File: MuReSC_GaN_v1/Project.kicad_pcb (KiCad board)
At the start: 2 copper layers, 19 parts, among them IC1 STM32G474RET6, IC10 UCC12040DVE, IC2 TPSM5601R5HRDAR, IC3 ISO7720FQDQ1, IC4 ISO7720FQDQ1, IC5 ISO7720FQDQ1, IC6 ISO7720FQDQ1, IC7 UCC12040DVE, IC8 UCC12040DVE, IC9 UCC12040DVE, J1 62000211121, J2 62000211121, J3 691214110002, J4 691214110002, J5 691214110002, J6 691214110002

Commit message: finito schema
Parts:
- removed J5, J6: 691214110002, SamacSys_Parts:691214110002
- added BEAD1: BLM15AG601SZ1D, SamacSys_Parts:NFZ15SG152SN10B, F.Cu at (131.7, 147.4)
- added BEAD2: BLM15AG601SZ1D, SamacSys_Parts:NFZ15SG152SN10B, F.Cu at (131.7, 149.9)
- added C1: C1812C124J1GACTU, SamacSys_Parts:C1812, F.Cu at (127.5, 136.8)
- added C2: C1206C821J1GACTU, SamacSys_Parts:C1206, F.Cu at (100.9, 148.9)
- added C3: C1812C105K1RACTU, SamacSys_Parts:C1812, F.Cu at (127.5, 143.1)
- added CCV1: C1210C107M8PACTU, SamacSys_Parts:C1210, F.Cu at (113.3, 92.3)
- added CCV2: C1210C107M8PACTU, SamacSys_Parts:C1210, F.Cu at (113.3, 97.9)
- added CD1: GRT155R70J105KE01D, SamacSys_Parts:CAPC1005X55N, F.Cu at (106.6, 130.3)
- added CD2: GRT155R70J105KE01D, SamacSys_Parts:CAPC1005X55N, F.Cu at (106.6, 132.3)
- added CD3: GRT155R70J105KE01D, SamacSys_Parts:CAPC1005X55N, F.Cu at (106.6, 134.3)
- added CD4: GRT155R70J105KE01D, SamacSys_Parts:CAPC1005X55N, F.Cu at (106.6, 136.2)
- added CFT1: NFM15PC104R1A3D, SamacSys_Parts:NFM15CC222D1A3D, F.Cu at (132.3, 109.8)
- added CFT2: NFM15PC104R1A3D, SamacSys_Parts:NFM15CC222D1A3D, F.Cu at (132.3, 112.6)
- added CFT3: NFM15PC104R1A3D, SamacSys_Parts:NFM15CC222D1A3D, F.Cu at (132.3, 115.5)
- added CFT4: NFM15PC104R1A3D, SamacSys_Parts:NFM15CC222D1A3D, F.Cu at (132.3, 118.3)
- added CIN1: GRJ31CZ72A475KE01L, SamacSys_Parts:CAPC3216X190N, F.Cu at (119.3, 91.2)
- added CIN2: GRJ31CZ72A475KE01L, SamacSys_Parts:CAPC3216X190N, F.Cu at (119.3, 94.5)
- added CISOP1: GRT155R70J105KE01D, SamacSys_Parts:CAPC1005X55N, F.Cu at (106.6, 138.2)
- added CISOP2: GRT155R70J105KE01D, SamacSys_Parts:CAPC1005X55N, F.Cu at (106.6, 140.2)
- added CISOP3: GRT155R70J105KE01D, SamacSys_Parts:CAPC1005X55N, F.Cu at (106.6, 142.2)
- added CISOP4: GRT155R70J105KE01D, SamacSys_Parts:CAPC1005X55N, F.Cu at (106.6, 144.1)
- added CISOS1: GRT155R70J105KE01D, SamacSys_Parts:CAPC1005X55N, F.Cu at (109.5, 130.3)
- added CISOS2: GRT155R70J105KE01D, SamacSys_Parts:CAPC1005X55N, F.Cu at (109.5, 132.3)
- added CISOS3: GRT155R70J105KE01D, SamacSys_Parts:CAPC1005X55N, F.Cu at (109.5, 134.3)
- added CISOS4: GRT155R70J105KE01D, SamacSys_Parts:CAPC1005X55N, F.Cu at (109.5, 136.2)
- added CLD1: GRM155Z71A105KE01J, SamacSys_Parts:CAPC1005X55N, F.Cu at (121.5, 97.1)
- added CLD2: GRT155R70J105KE01D, SamacSys_Parts:CAPC1005X55N, F.Cu at (121.5, 99.1)
- added CM0: GRM155R61A475MEAAD, SamacSys_Parts:CAPC1005X55N, F.Cu at (109.5, 138.2)
- added CM1: C0402C104K8RAC7867, SamacSys_Parts:CAPC1005X55N, F.Cu at (109.5, 140.2)
- added CM10: C0402C104K8RAC7867, SamacSys_Parts:CAPC1005X55N, F.Cu at (112.4, 142.2)
- added CM2: C0402C104K8RAC7867, SamacSys_Parts:CAPC1005X55N, F.Cu at (109.5, 142.2)
- added CM3: C0402C104K8RAC7867, SamacSys_Parts:CAPC1005X55N, F.Cu at (109.5, 144.1)
- added CM4: C0402C104K8RAC7867, SamacSys_Parts:CAPC1005X55N, F.Cu at (112.4, 130.3)
- added CM5: GRT155R70J105KE01D, SamacSys_Parts:CAPC1005X55N, F.Cu at (112.4, 132.3)
- added CM6: C0402C104K8RAC7867, SamacSys_Parts:CAPC1005X55N, F.Cu at (112.4, 134.3)
- added CM7: C0402C104K8RAC7867, SamacSys_Parts:CAPC1005X55N, F.Cu at (112.4, 136.2)
- added CM8: GRT155R70J105KE01D, SamacSys_Parts:CAPC1005X55N, F.Cu at (112.4, 138.2)
- added CM9: C0402C104K8RAC7867, SamacSys_Parts:CAPC1005X55N, F.Cu at (112.4, 140.2)
- added COH1: GJM0335C1E6R8DB01D, SamacSys_Parts:CAPC0603X33N, F.Cu at (113.1, 148.5)
- added COH2: GJM0335C1E6R8DB01D, SamacSys_Parts:CAPC0603X33N, F.Cu at (113.1, 150.3)
- added COL1: C, Capacitor_SMD:C_0201_0603Metric_Pad0.64x0.40mm_HandSolder, F.Cu at (93.7, 146.8)
- added COL2: C, Capacitor_SMD:C_0201_0603Metric_Pad0.64x0.40mm_HandSolder, F.Cu at (93.7, 148.6)
- added CTP1: C0402C104K8RAC7867, SamacSys_Parts:CAPC1005X55N, F.Cu at (112.4, 144.1)
- added CTP2: C0402C104K8RAC7867, SamacSys_Parts:CAPC1005X55N, F.Cu at (115.2, 130.3)
- added CTP3: C0402C104K8RAC7867, SamacSys_Parts:CAPC1005X55N, F.Cu at (115.2, 132.3)
- added CTP4: C0402C104K8RAC7867, SamacSys_Parts:CAPC1005X55N, F.Cu at (115.2, 134.3)
- added CTPB1: C0603C106M8PAC7411, SamacSys_Parts:C0603, F.Cu at (94.9, 110.3)
- added CTPB2: C0603C106M8PAC7411, SamacSys_Parts:C0603, F.Cu at (94.9, 114.1)
- added CTPB3: C0603C106M8PAC7411, SamacSys_Parts:C0603, F.Cu at (94.9, 118.0)
- added CTPB4: C0603C106M8PAC7411, SamacSys_Parts:C0603, F.Cu at (94.9, 121.8)
- added CTS1: C0402C104K8RAC7867, SamacSys_Parts:CAPC1005X55N, F.Cu at (115.2, 136.2)
- added CTS2: C0402C104K8RAC7867, SamacSys_Parts:CAPC1005X55N, F.Cu at (115.2, 138.2)
- added CTS3: C0402C104K8RAC7867, SamacSys_Parts:CAPC1005X55N, F.Cu at (115.2, 140.2)
- added CTS4: C0402C104K8RAC7867, SamacSys_Parts:CAPC1005X55N, F.Cu at (115.2, 142.2)
- added CTSB1: C0603C106M8PAC7411, SamacSys_Parts:C0603, F.Cu at (94.9, 125.7)
- added CTSB2: C0603C106M8PAC7411, SamacSys_Parts:C0603, F.Cu at (94.9, 129.5)
- added CTSB3: C0603C106M8PAC7411, SamacSys_Parts:C0603, F.Cu at (94.9, 133.4)
- added CTSB4: C0603C106M8PAC7411, SamacSys_Parts:C0603, F.Cu at (94.9, 137.2)
- added D1: ESDALC6V1-1U2, SamacSys_Parts:ESDALC6V11U2, F.Cu at (94.5, 140.9)
- added D2: ESDALC6V1-1U2, SamacSys_Parts:ESDALC6V11U2, F.Cu at (94.5, 144.3)
- added IC11: LMG1020YFFR, SamacSys_Parts:BGA6C40P2X3_86X126X62, F.Cu at (118.6, 131.5)
- added IC12: LMG1020YFFR, SamacSys_Parts:BGA6C40P2X3_86X126X62, F.Cu at (122.6, 131.5)
- added IC13: LMG1020YFFR, SamacSys_Parts:BGA6C40P2X3_86X126X62, F.Cu at (126.5, 131.5)
- added IC14: LMG1020YFFR, SamacSys_Parts:BGA6C40P2X3_86X126X62, F.Cu at (130.5, 131.5)
- added L1: L, Inductor_SMD:L_0603_1608Metric, F.Cu at (113.9, 146.4)
- added P1: 691214110002, SamacSys_Parts:691214110002, F.Cu at (108.7, 113.9)
- added P2: 691214110002, SamacSys_Parts:691214110002, F.Cu at (108.7, 124.4)
- added Q1: GS61004B-TR, SamacSys_Parts:GS61004BTR, F.Cu at (101.3, 112.1)
- added Q2: GS61004B-TR, SamacSys_Parts:GS61004BTR, F.Cu at (101.3, 119.6)
- added Q3: GS61004B-TR, SamacSys_Parts:GS61004BTR, F.Cu at (101.3, 127.1)
- added Q4: GS61004B-TR, SamacSys_Parts:GS61004BTR, F.Cu at (101.3, 134.6)
- added RF1: MCS04020D1002BE000, SamacSys_Parts:RESC1005X37N, F.Cu at (118.3, 97.2)
- added RF2: MCS04020D2491BE000, SamacSys_Parts:RESC1005X37N, F.Cu at (118.3, 99.3)
- added RH1: MCS0402MC1008FE000, SamacSys_Parts:RESC1005X37N, F.Cu at (118.4, 134.8)
- added RH2: MCS0402MC1008FE000, SamacSys_Parts:RESC1005X37N, F.Cu at (118.4, 136.9)
- added RH3: MCS0402MC1008FE000, SamacSys_Parts:RESC1005X37N, F.Cu at (118.4, 139.1)
- added RH4: MCS0402MC1008FE000, SamacSys_Parts:RESC1005X37N, F.Cu at (118.4, 141.2)
- added RL1: MCS0402MC1008FE000, SamacSys_Parts:RESC1005X37N, F.Cu at (118.4, 143.4)
- added RL2: MCS0402MC1008FE000, SamacSys_Parts:RESC1005X37N, F.Cu at (118.4, 145.5)
- added RL3: MCS0402MC1008FE000, SamacSys_Parts:RESC1005X37N, F.Cu at (121.7, 134.8)
- added RL4: MCS0402MC1008FE000, SamacSys_Parts:RESC1005X37N, F.Cu at (121.7, 136.9)
- added RM1: MCS04020D1002BE000, SamacSys_Parts:RESC1005X37N, F.Cu at (121.7, 139.1)
- added RS1: R, Resistor_SMD:R_0603_1608Metric_Pad0.98x0.95mm_HandSolder, F.Cu at (117.9, 109.6)
- added RS2: R, Resistor_SMD:R_0603_1608Metric_Pad0.98x0.95mm_HandSolder, F.Cu at (117.9, 112.1)
- added RS3: R, Resistor_SMD:R_0603_1608Metric_Pad0.98x0.95mm_HandSolder, F.Cu at (117.9, 114.6)
- added RS4: R, Resistor_SMD:R_0603_1608Metric_Pad0.98x0.95mm_HandSolder, F.Cu at (117.9, 117.1)
- added RS5: R, Resistor_SMD:R_0603_1608Metric_Pad0.98x0.95mm_HandSolder, F.Cu at (117.9, 119.7)
- added RS6: R, Resistor_SMD:R_0603_1608Metric_Pad0.98x0.95mm_HandSolder, F.Cu at (117.9, 122.2)
- added RS7: R, Resistor_SMD:R_0603_1608Metric_Pad0.98x0.95mm_HandSolder, F.Cu at (117.9, 124.7)
- added RS8: R, Resistor_SMD:R_0603_1608Metric_Pad0.98x0.95mm_HandSolder, F.Cu at (117.9, 127.2)
- added RUB1: MCS04020C3300FE000, SamacSys_Parts:RESC1005X37N, F.Cu at (121.7, 141.2)
- added RUB2: MCS04020C1003FE000, SamacSys_Parts:RESC1005X37N, F.Cu at (121.7, 143.4)
- added S1: PTS526_SK15_SMTR2_LFS, SamacSys_Parts:PTS526SK15SMTR2LFS, F.Cu at (125.6, 112.5)
- added S2: PTS526_SK15_SMTR2_LFS, SamacSys_Parts:PTS526SK15SMTR2LFS, F.Cu at (125.6, 120.8)
- added Y1: NX3215SA-32.768K-STD-MUS-2, SamacSys_Parts:NX3215SA32768KSTDMUS2, F.Cu at (126.7, 148.6)
- added Y2: NX3225SA-24.000MHZ-STD-CSR-1, SamacSys_Parts:NX3225SA24000MHZSTDCSR1, F.Cu at (108.5, 148.1)
- added Z3: TSZU52C3V3_RGG, SamacSys_Parts:TSZU52C3V3RGG, F.Cu at (100.0, 140.4)
- added Z4: TSZU52C3V3_RGG, SamacSys_Parts:TSZU52C3V3RGG, F.Cu at (100.0, 144.5)
- J1: value 62000211121 -> 62000211121_x6; footprint SamacSys_Parts:62000211121 -> SamacSys_Parts:62000211121_x6
- J3, J4: value 691214110002 -> 62000211121_x1; footprint SamacSys_Parts:691214110002 -> SamacSys_Parts:62000211121_x1
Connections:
- IC1 pad 1: unconnected-(IC1-VBAT-Pad1) -> /VDD3V3
- IC1 pad 12: unconnected-(IC1-PA0-Pad12) -> /ADC1_IN1
- IC1 pad 13: unconnected-(IC1-PA1-Pad13) -> /ADC2_IN2
- IC1 pad 14: unconnected-(IC1-PA2-Pad14) -> /STLINK_RX
- IC1 pad 15: unconnected-(IC1-VSS_1-Pad15) -> GND
- IC1 pad 16: unconnected-(IC1-VDD_1-Pad16) -> /VDD3V3
- IC1 pad 17: unconnected-(IC1-PA3-Pad17) -> /STLINK_TX
- IC1 pad 18: unconnected-(IC1-PA4-Pad18) -> /COMP1_INM
- IC1 pad 19: unconnected-(IC1-PA5-Pad19) -> /COMP2_INM
- IC1 pad 2: unconnected-(IC1-PC13-Pad2) -> /UBUTT
- IC1 pad 21: unconnected-(IC1-PA7-Pad21) -> /COMP2_INP
- IC1 pad 25: unconnected-(IC1-PB1-Pad25) -> /COMP1_INP
- IC1 pad 27: unconnected-(IC1-VSSA-Pad27) -> GND
- IC1 pad 28: unconnected-(IC1-VREF+-Pad28) -> /VREFP
- IC1 pad 29: unconnected-(IC1-VDDA-Pad29) -> Net-(IC1-VDDA)
- IC1 pad 3: unconnected-(IC1-PC14-OSC32_IN-Pad3) -> /OSC32_IN
- IC1 pad 31: unconnected-(IC1-VSS_2-Pad31) -> GND
- IC1 pad 32: unconnected-(IC1-VDD_2-Pad32) -> /VDD3V3
- IC1 pad 34: unconnected-(IC1-PB12-Pad34) -> /HRTIM1_CHC1
- IC1 pad 35: unconnected-(IC1-PB13-Pad35) -> /HRTIM1_CHC2
- IC1 pad 36: unconnected-(IC1-PB14-Pad36) -> /HRTIM1_CHD1
- IC1 pad 37: unconnected-(IC1-PB15-Pad37) -> /HRTIM1_CHD2
- IC1 pad 4: unconnected-(IC1-PC15-OSC32_OUT-Pad4) -> /OSC32_OUT
- IC1 pad 42: unconnected-(IC1-PA8-Pad42) -> /HRTIM1_CHA1
- IC1 pad 43: unconnected-(IC1-PA9-Pad43) -> /HRTIM1_CHA2
- IC1 pad 44: unconnected-(IC1-PA10-Pad44) -> /HRTIM1_CHB1
- IC1 pad 45: unconnected-(IC1-PA11-Pad45) -> /HRTIM1_CHB2
- IC1 pad 47: unconnected-(IC1-VSS_3-Pad47) -> GND
- IC1 pad 48: unconnected-(IC1-VDD_3-Pad48) -> /VDD3V3
- IC1 pad 49: unconnected-(IC1-PA13-Pad49) -> /T_SWDIO
- IC1 pad 5: unconnected-(IC1-PF0-OSC_IN-Pad5) -> /OSC24_IN
- IC1 pad 50: unconnected-(IC1-PA14-Pad50) -> /T_SWCLK
- IC1 pad 6: unconnected-(IC1-PF1-OSC_OUT-Pad6) -> /OSC24_OUT
- IC1 pad 61: unconnected-(IC1-PB8-BOOT0-Pad61) -> Net-(IC1-PB8-BOOT0)
- IC1 pad 63: unconnected-(IC1-VSS_4-Pad63) -> GND
- IC1 pad 64: unconnected-(IC1-VDD_4-Pad64) -> /VDD3V3
- IC1 pad 7: unconnected-(IC1-PG10-NRST-Pad7) -> /NRST
- IC10 pad 1: unconnected-(IC10-EN-Pad1) -> /VDD5V
- IC10 pad 10: unconnected-(IC10-NC_4-Pad10) -> GND
- IC10 pad 11: unconnected-(IC10-NC_5-Pad11) -> GND
- IC10 pad 12: unconnected-(IC10-NC_6-Pad12) -> GND
- IC10 pad 13: unconnected-(IC10-SEL-Pad13) -> /VDDI4
- IC10 pad 14: unconnected-(IC10-VISO-Pad14) -> /VDDI4
- IC10 pad 15: unconnected-(IC10-GNDS_2-Pad15) -> GND
- IC10 pad 16: unconnected-(IC10-GNDS_3-Pad16) -> GND
- IC10 pad 2: unconnected-(IC10-GNDP-Pad2) -> GND
- IC10 pad 3: unconnected-(IC10-VINP-Pad3) -> /VDD5V
- IC10 pad 4: unconnected-(IC10-SYNC-Pad4) -> GND
- IC10 pad 6: unconnected-(IC10-NC_1-Pad6) -> GND
- IC10 pad 7: unconnected-(IC10-NC_2-Pad7) -> GND
- IC10 pad 8: unconnected-(IC10-NC_3-Pad8) -> GND
- IC10 pad 9: unconnected-(IC10-GNDS_1-Pad9) -> GND
- IC2 pad 1: unconnected-(IC2-VIN_1-Pad1) -> /VDD48V
- IC2 pad 10: unconnected-(IC2-AGND-Pad10) -> GND
- IC2 pad 12: unconnected-(IC2-PGOOD-Pad12) -> GND
- IC2 pad 14: unconnected-(IC2-VIN_2-Pad14) -> /VDD48V
- IC2 pad 2: unconnected-(IC2-EN-Pad2) -> /VDD48V
- IC2 pad 7: unconnected-(IC2-VOUT_1-Pad7) -> /VDD5V
- IC2 pad 8: unconnected-(IC2-VOUT_2-Pad8) -> /VDD5V
- IC2 pad 9: unconnected-(IC2-FB-Pad9) -> /TPSFB
- IC3 pad 1: unconnected-(IC3-VCC1-Pad1) -> /VDD3V3
- IC3 pad 2: unconnected-(IC3-INA-Pad2) -> /HRTIM1_CHA1
- IC3 pad 3: unconnected-(IC3-INB-Pad3) -> /HRTIM1_CHA2
- IC3 pad 4: unconnected-(IC3-GND1-Pad4) -> GND
- IC3 pad 5: unconnected-(IC3-GND2-Pad5) -> /S1
- IC3 pad 6: unconnected-(IC3-OUTB-Pad6) -> /INN1
- IC3 pad 7: unconnected-(IC3-OUTA-Pad7) -> /INP1
- IC3 pad 8: unconnected-(IC3-VCC2-Pad8) -> /VDDI1
- IC4 pad 1: unconnected-(IC4-VCC1-Pad1) -> /VDD3V3
- IC4 pad 2: unconnected-(IC4-INA-Pad2) -> /HRTIM1_CHB1
- IC4 pad 3: unconnected-(IC4-INB-Pad3) -> /HRTIM1_CHB2
- IC4 pad 4: unconnected-(IC4-GND1-Pad4) -> GND
- IC4 pad 5: unconnected-(IC4-GND2-Pad5) -> /S2
- IC4 pad 6: unconnected-(IC4-OUTB-Pad6) -> /INN2
- IC4 pad 7: unconnected-(IC4-OUTA-Pad7) -> /INP2
- IC4 pad 8: unconnected-(IC4-VCC2-Pad8) -> /VDDI2
- IC5 pad 1: unconnected-(IC5-VCC1-Pad1) -> /VDD3V3
- IC5 pad 2: unconnected-(IC5-INA-Pad2) -> /HRTIM1_CHC1
- IC5 pad 3: unconnected-(IC5-INB-Pad3) -> /HRTIM1_CHC2
- IC5 pad 4: unconnected-(IC5-GND1-Pad4) -> GND
- IC5 pad 5: unconnected-(IC5-GND2-Pad5) -> /S3
- IC5 pad 6: unconnected-(IC5-OUTB-Pad6) -> /INN3
- IC5 pad 7: unconnected-(IC5-OUTA-Pad7) -> /INP3
- IC5 pad 8: unconnected-(IC5-VCC2-Pad8) -> /VDDI3
- IC6 pad 1: unconnected-(IC6-VCC1-Pad1) -> /VDD3V3
- IC6 pad 2: unconnected-(IC6-INA-Pad2) -> /HRTIM1_CHD1
- IC6 pad 3: unconnected-(IC6-INB-Pad3) -> /HRTIM1_CHD2
- IC6 pad 4: unconnected-(IC6-GND1-Pad4) -> GND
- IC6 pad 5: unconnected-(IC6-GND2-Pad5) -> GND
- IC6 pad 6: unconnected-(IC6-OUTB-Pad6) -> /INN4
- IC6 pad 7: unconnected-(IC6-OUTA-Pad7) -> /INP4
- IC6 pad 8: unconnected-(IC6-VCC2-Pad8) -> /VDDI4
- IC7 pad 1: unconnected-(IC7-EN-Pad1) -> /VDD5V
- IC7 pad 10: unconnected-(IC7-NC_4-Pad10) -> /S1
- IC7 pad 11: unconnected-(IC7-NC_5-Pad11) -> /S1
- IC7 pad 12: unconnected-(IC7-NC_6-Pad12) -> /S1
- IC7 pad 13: unconnected-(IC7-SEL-Pad13) -> /VDDI1
- IC7 pad 14: unconnected-(IC7-VISO-Pad14) -> /VDDI1
- IC7 pad 15: unconnected-(IC7-GNDS_2-Pad15) -> /S1
- IC7 pad 16: unconnected-(IC7-GNDS_3-Pad16) -> /S1
- IC7 pad 2: unconnected-(IC7-GNDP-Pad2) -> GND
- IC7 pad 3: unconnected-(IC7-VINP-Pad3) -> /VDD5V
- IC7 pad 4: unconnected-(IC7-SYNC-Pad4) -> GND
- IC7 pad 6: unconnected-(IC7-NC_1-Pad6) -> GND
- IC7 pad 7: unconnected-(IC7-NC_2-Pad7) -> GND
- IC7 pad 8: unconnected-(IC7-NC_3-Pad8) -> GND
- IC7 pad 9: unconnected-(IC7-GNDS_1-Pad9) -> /S1
- IC8 pad 1: unconnected-(IC8-EN-Pad1) -> /VDD5V
- IC8 pad 10: unconnected-(IC8-NC_4-Pad10) -> /S2
- IC8 pad 11: unconnected-(IC8-NC_5-Pad11) -> /S2
- IC8 pad 12: unconnected-(IC8-NC_6-Pad12) -> /S2
- IC8 pad 13: unconnected-(IC8-SEL-Pad13) -> /VDDI2
- IC8 pad 14: unconnected-(IC8-VISO-Pad14) -> /VDDI2
- IC8 pad 15: unconnected-(IC8-GNDS_2-Pad15) -> /S2
- IC8 pad 16: unconnected-(IC8-GNDS_3-Pad16) -> /S2
- IC8 pad 2: unconnected-(IC8-GNDP-Pad2) -> GND
- IC8 pad 3: unconnected-(IC8-VINP-Pad3) -> /VDD5V
- IC8 pad 4: unconnected-(IC8-SYNC-Pad4) -> GND
- IC8 pad 6: unconnected-(IC8-NC_1-Pad6) -> GND
- IC8 pad 7: unconnected-(IC8-NC_2-Pad7) -> GND
- IC8 pad 8: unconnected-(IC8-NC_3-Pad8) -> GND
- IC8 pad 9: unconnected-(IC8-GNDS_1-Pad9) -> /S2
- IC9 pad 1: unconnected-(IC9-EN-Pad1) -> /VDD5V
- IC9 pad 10: unconnected-(IC9-NC_4-Pad10) -> /S3
- IC9 pad 11: unconnected-(IC9-NC_5-Pad11) -> /S3
- IC9 pad 12: unconnected-(IC9-NC_6-Pad12) -> /S3
- IC9 pad 13: unconnected-(IC9-SEL-Pad13) -> /VDDI3
- IC9 pad 14: unconnected-(IC9-VISO-Pad14) -> /VDDI3
- IC9 pad 15: unconnected-(IC9-GNDS_2-Pad15) -> /S3
- IC9 pad 16: unconnected-(IC9-GNDS_3-Pad16) -> /S3
- IC9 pad 2: unconnected-(IC9-GNDP-Pad2) -> GND
- IC9 pad 3: unconnected-(IC9-VINP-Pad3) -> /VDD5V
- IC9 pad 4: unconnected-(IC9-SYNC-Pad4) -> GND
- IC9 pad 6: unconnected-(IC9-NC_1-Pad6) -> GND
- IC9 pad 7: unconnected-(IC9-NC_2-Pad7) -> GND
- IC9 pad 8: unconnected-(IC9-NC_3-Pad8) -> GND
- IC9 pad 9: unconnected-(IC9-GNDS_1-Pad9) -> /S3
- J1 pad 1: unconnected-(J1-Pad1) -> /VDD3V3
- J1 pad 2: unconnected-(J1-Pad2) -> /T_SWCLK
- J2 pad 1: unconnected-(J2-Pad1) -> /STLINK_TX
- J2 pad 2: unconnected-(J2-Pad2) -> /STLINK_RX
- J3 pad 1: unconnected-(J3-Pad1) -> /COMP1_INM
- J4 pad 1: unconnected-(J4-Pad1) -> /COMP2_INM
- PS1 pad 1: unconnected-(PS1-EN-Pad1) -> /VDD5V
- PS1 pad 2: unconnected-(PS1-GND-Pad2) -> GND
- PS1 pad 4: unconnected-(PS1-VOUT-Pad4) -> /VDD3V3
- PS1 pad 6: unconnected-(PS1-VIN-Pad6) -> /VDD5V
- PS1 pad 7: unconnected-(PS1-PAD-Pad7) -> GND
- Z1 pad 1: unconnected-(Z1-K-Pad1) -> /ADC1_IN1
- Z1 pad 2: unconnected-(Z1-A-Pad2) -> GND
- Z2 pad 1: unconnected-(Z2-K-Pad1) -> /COMP1_INP
- Z2 pad 2: unconnected-(Z2-A-Pad2) -> GND

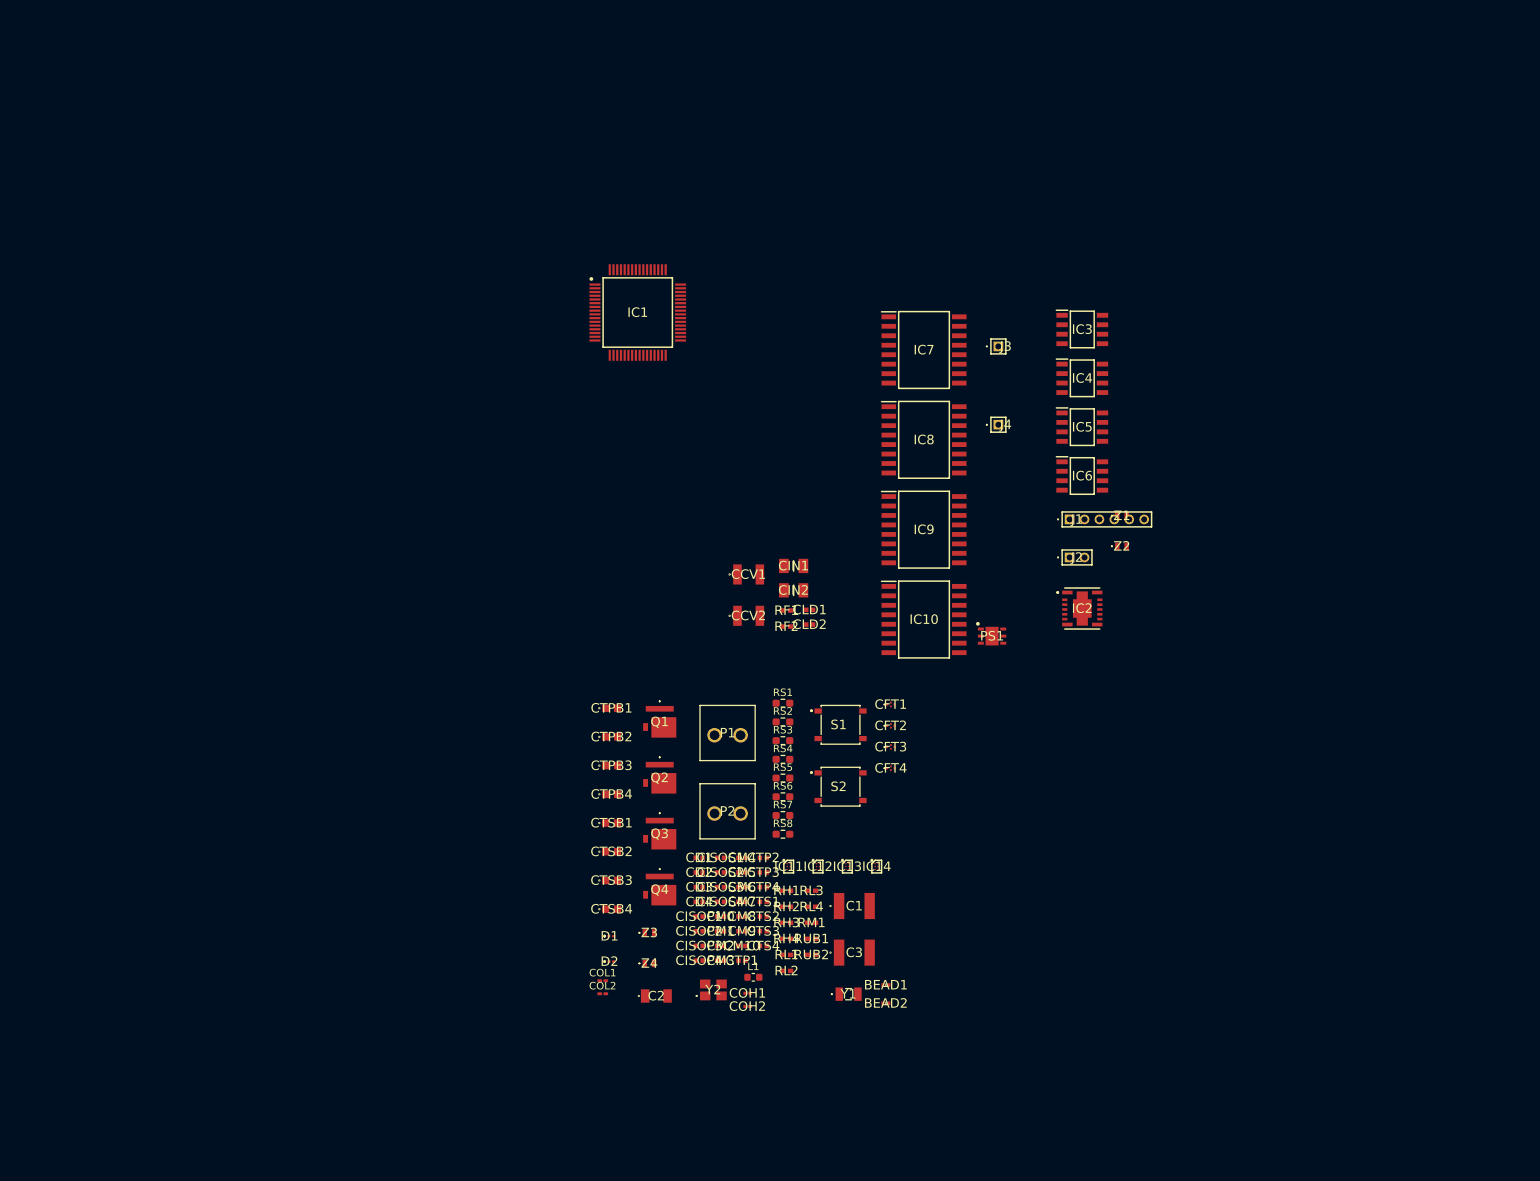
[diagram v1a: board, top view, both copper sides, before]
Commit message: schematic finished + start layout
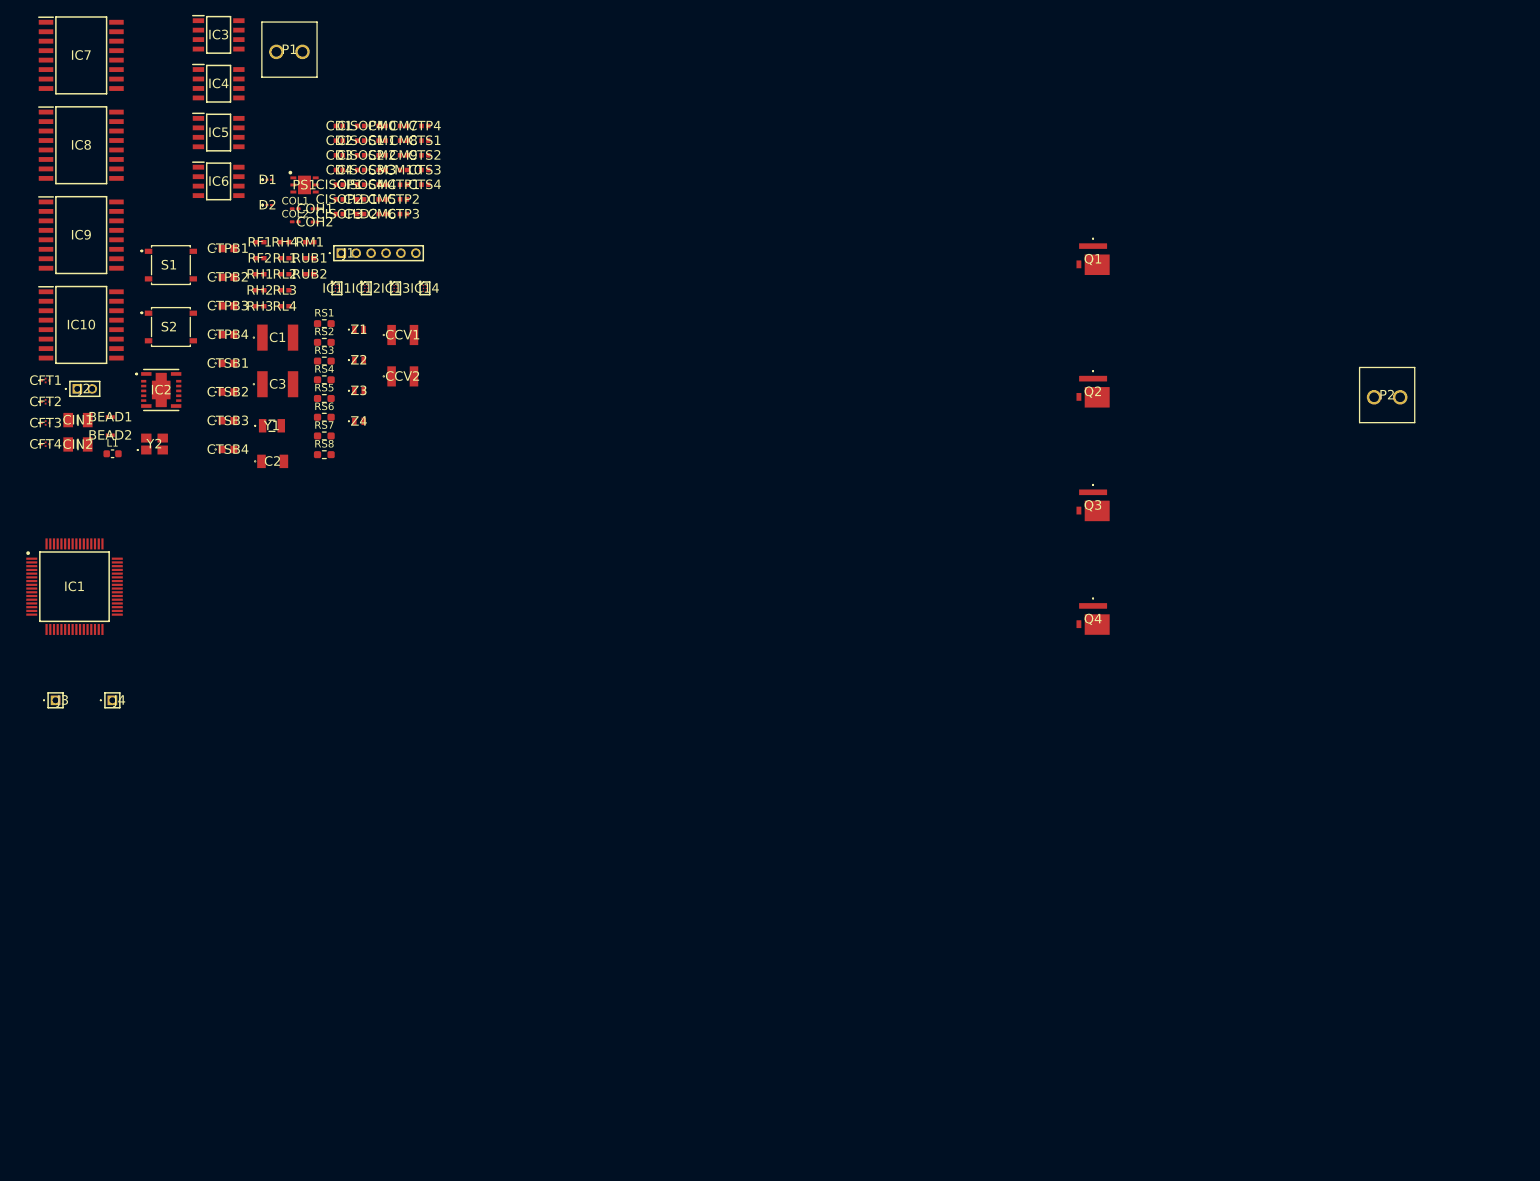
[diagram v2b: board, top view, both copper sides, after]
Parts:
- moved J3 135.1 mm to (20.3, 109.2)
- moved J2 135.0 mm to (23.2, 67.5)
- moved BEAD1 128.9 mm to (27.7, 71.2)
- moved BEAD2 128.9 mm to (27.7, 73.7)
- moved IC2 127.0 mm to (34.5, 67.6)
- moved J4 124.4 mm to (27.9, 109.2)
- moved IC3 122.4 mm to (42.2, 20.0)
- moved IC4 122.4 mm to (42.2, 26.5)
- moved IC5 122.4 mm to (42.2, 33.1)
- moved IC6 122.4 mm to (42.2, 39.6)
- moved CFT1 121.4 mm to (19.0, 66.3)
- moved CFT2 121.4 mm to (19.0, 69.2)
- moved CFT3 121.4 mm to (19.0, 72.0)
- moved CFT4 121.4 mm to (19.0, 74.9)
- moved CISOP4 120.8 mm to (61.2, 32.2)
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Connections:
- IC2 pad 15: unconnected-(IC2-PGND_1-Pad15) -> GND
- IC2 pad A15: unconnected-(IC2-PGND_2-PadA15) -> GND
- IC2 pad B15: unconnected-(IC2-PGND_3-PadB15) -> GND
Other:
- copper layers 2 -> 4

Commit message: prova
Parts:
- moved P2 11.4 mm to (202.2, 78.8)
- moved Q2 11.4 mm to (164.5, 78.0)
- moved Q3 11.4 mm to (164.5, 93.3)
- moved Q1 11.4 mm to (164.5, 60.3)
- moved Q4 11.4 mm to (164.5, 108.5)
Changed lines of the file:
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@@
   )
   (footprint "SamacSys_Parts:GS61004BTR" (layer "F.Cu")
-    (at 159.47 83.07)
+    (at 164.46 93.28)
     (descr "GS61004B-TR")
     (tags "Transistor E-mode GaN (3-Pin)")
@@
   )
   (footprint "SamacSys_Parts:GS61004BTR" (layer "F.Cu")
-    (at 159.47 67.83)
+    (at 164.46 78.04)
     (descr "GS61004B-TR")
     (tags "Transistor E-mode GaN (3-Pin)")
@@
   )
   (footprint "SamacSys_Parts:GS61004BTR" (layer "F.Cu")
-    (at 159.47 50.05)
+    (at 164.46 60.26)
     (descr "GS61004B-TR")
     (tags "Transistor E-mode GaN (3-Pin)")
@@
   )
   (footprint "SamacSys_Parts:GS61004BTR" (layer "F.Cu")
-    (at 159.47 98.31)
+    (at 164.46 108.52)
     (descr "GS61004B-TR")
     (tags "Transistor E-mode GaN (3-Pin)")
@@
   )
   (footprint "SamacSys_Parts:691214110002" (layer "F.Cu")
-    (at 197.16 68.58)
+    (at 202.15 78.79)
     (descr "691214110002-2")
     (tags "Connector")

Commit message: placement
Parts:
- CTP1, CTP2, CTP3, CTP4, CTPB1, CTPB2, CTPB3, CTPB4, CTS1, CTS2, CTS3, CTS4, CTSB1, CTSB2, CTSB3, CTSB4, IC10, IC7, IC8, IC9: moved to B.Cu
- L1: value L -> 2222SQ-221GEC; footprint Inductor_SMD:L_0603_1608Metric -> SamacSys_Parts:2222SQ221GEC
- moved L1 161.0 mm to (188.0, 94.0), turned to 90 degrees
- moved C3 154.0 mm to (203.2, 83.8), turned to -90 degrees
- moved C1 139.4 mm to (188.0, 81.3), turned to -90 degrees
- moved CFT4 135.4 mm to (151.1, 104.5)
- moved CFT3 133.3 mm to (151.1, 89.9)
- moved CFT1 132.8 mm to (151.8, 62.5)
- moved CFT2 132.2 mm to (151.1, 73.4)
- moved C2 126.4 mm to (175.3, 88.9), turned to -90 degrees
- moved IC10 124.3 mm to (136.2, 111.8)
- moved RH4 123.7 mm to (158.8, 108.6)
- moved IC9 123.3 mm to (136.9, 95.9)
- moved IC8 121.6 mm to (136.9, 79.4)
- moved RL4 120.6 mm to (158.8, 110.5)
- moved IC7 119.4 mm to (136.9, 61.0)
- moved IC6 118.6 mm to (136.4, 111.8)
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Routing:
- net /TPSFB: track 0.00 -> 4.93 mm
- net /VDD5V: track 0.00 -> 3.22 mm

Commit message: layout prosegue
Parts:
- moved J3 78.8 mm to (23.5, 113.7), turned to 180 degrees
- moved J4 75.8 mm to (27.9, 113.7), turned to 180 degrees
- moved J1 70.3 mm to (19.1, 97.3), turned to -90 degrees
- moved CLD1 63.0 mm to (44.1, 91.7)
- moved CLD2 63.0 mm to (37.8, 91.8)
- moved PS1 63.0 mm to (40.6, 90.8)
- moved J2 62.4 mm to (19.1, 113.4), turned to 90 degrees
- moved S1 33.8 mm to (21.0, 91.4), turned to 180 degrees
- moved D1 33.8 mm to (27.8, 91.4), turned to 90 degrees
- moved CM9 33.2 mm to (30.5, 91.4), turned to 90 degrees
- moved CM6 17.5 mm to (33.7, 112.2), turned to 90 degrees
- moved D2 16.8 mm to (28.1, 86.0)
- moved CM10 16.5 mm to (28.9, 82.8), turned to 180 degrees
- moved BEAD2 15.9 mm to (34.7, 109.9)
- moved RUB1 15.8 mm to (30.7, 85.2), turned to -90 degrees
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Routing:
- net GND: track 0.00 -> 44.4 mm, vias 0 -> 99
- net /NRST: track 0.00 -> 41.2 mm
- net /UBUTT: track 0.00 -> 30.5 mm, vias 0 -> 2
- net /T_SWDIO: track 0.00 -> 30.1 mm, vias 0 -> 1
- net /T_SWCLK: track 0.00 -> 29.9 mm, vias 0 -> 1
- net /VDD3V3: track 0.00 -> 18.2 mm, vias 0 -> 49
- net /STLINK_RX: track 0.00 -> 18.2 mm
- net /STLINK_TX: track 0.00 -> 15.6 mm
- net /OSC24_OUT: track 0.00 -> 13.5 mm
- net /COMP1_INM: track 0.00 -> 12.4 mm
- net /OSC24_IN: track 0.00 -> 11.0 mm
- net /COMP2_INM: track 0.00 -> 9.31 mm
- net /OSC32_IN: track 0.00 -> 8.22 mm
- net /OSC32_OUT: track 0.00 -> 8.18 mm
- net Net-(CM10-Pad1): track 0.00 -> 4.34 mm
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- added copper zone on F.Cu, net /VDD3V3
- added copper zone on In2.Cu, net /VDD3V3
- added copper zone on F.Cu, net /VREFP
- added copper zone on F.Cu, net GND
- added copper zone on In1.Cu, net GND
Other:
- board outline added: 36.2 x 36.8 mm

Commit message: lauyout update
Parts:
- moved P1 97.6 mm to (64.4, 83.8)
- moved CISOS1 91.7 mm to (56.3, 90.7), turned to 90 degrees
- moved IC3 90.4 mm to (51.7, 92.8)
- moved CISOS2 89.0 mm to (56.8, 97.3), turned to -90 degrees
- moved CISOS3 87.3 mm to (56.8, 103.8), turned to -90 degrees
- moved IC4 86.8 mm to (51.9, 99.4)
- moved CISOS4 86.3 mm to (56.8, 110.6), turned to -90 degrees
- moved IC5 85.3 mm to (51.9, 106.2)
- moved IC6 84.5 mm to (51.9, 112.9)
- moved CISOP1 82.8 mm to (49.8, 89.5)
- moved CISOP2 80.7 mm to (50.1, 96.1)
- moved CISOP3 78.4 mm to (50.3, 102.7)
- moved CISOP4 77.9 mm to (50.0, 109.6)
- moved RF1 76.3 mm to (45.3, 87.9), turned to 0 degrees
- moved RF2 75.0 mm to (48.8, 87.9), turned to 180 degrees
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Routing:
- net GND: track 44.4 -> 59.2 mm, vias 99 -> 181
- net /VDD5V: track 3.22 -> 1.87 mm, vias 0 -> 45
- net /VDD48V: track 0.00 -> 1.34 mm, vias 0 -> 28
- net /HRTIM1_CHB1: track 0.00 -> 0.80 mm
- added copper zone on F.Cu, net /VDD48V
- added copper zone on In2.Cu, net /VDD48V
- added copper zone on B.Cu, net /VDD5V
- added copper zone on F.Cu, net /VDD5V
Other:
- board size 36.2 x 36.8 mm -> 69.3 x 36.8 mm

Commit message: lauyout update
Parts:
- moved RH1 99.4 mm to (65.0, 92.0)
- moved RL1 99.2 mm to (65.0, 93.3)
- moved CD1 99.0 mm to (59.1, 93.9), turned to 0 degrees
- moved Q1 98.2 mm to (71.6, 92.4)
- moved IC11 98.0 mm to (61.9, 92.7)
- moved CFT1 97.3 mm to (59.2, 92.2)
- moved RH2 96.8 mm to (64.9, 100.3)
- moved RL2 96.7 mm to (64.9, 101.9)
- moved CFT2 95.7 mm to (59.3, 100.4)
- moved Q2 95.5 mm to (71.7, 101.0)
- moved IC12 95.1 mm to (62.1, 101.0)
- moved CD2 95.1 mm to (59.3, 102.1), turned to 0 degrees
- moved RL3 95.0 mm to (64.9, 109.3)
- moved RH3 95.0 mm to (65.0, 107.5)
- moved RL4 94.6 mm to (64.5, 117.6)
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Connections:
- net Net-(Q1-G) renamed /G1
- net Net-(Q2-G) renamed /G2
- net Net-(Q3-G) renamed /G3
- net Net-(Q4-G) renamed /G4
- IC3 pad 2: /HRTIM1_CHA1 -> /HRTIM1_CHB2
- IC3 pad 3: /HRTIM1_CHA2 -> /HRTIM1_CHB1
- IC4 pad 2: /HRTIM1_CHB1 -> /HRTIM1_CHA2
- IC4 pad 3: /HRTIM1_CHB2 -> /HRTIM1_CHA1
- IC5 pad 2: /HRTIM1_CHC1 -> /HRTIM1_CHD2
- IC5 pad 3: /HRTIM1_CHC2 -> /HRTIM1_CHD1
- IC6 pad 2: /HRTIM1_CHD1 -> /HRTIM1_CHC2
- IC6 pad 3: /HRTIM1_CHD2 -> /HRTIM1_CHC1
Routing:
- net GND: track 59.2 -> 288.4 mm, vias 181 -> 206
- net /S2: track 0.00 -> 56.0 mm, vias 0 -> 4
- net /S1: track 0.00 -> 54.2 mm, vias 0 -> 4
- net /S3: track 0.00 -> 53.6 mm, vias 0 -> 4
- net /VDD5V: track 1.87 -> 30.9 mm
- net /VDDI1: track 0.00 -> 19.5 mm, vias 0 -> 4
- net /VDDI2: track 0.00 -> 16.0 mm, vias 0 -> 4
- net /VDDI3: track 0.00 -> 15.6 mm, vias 0 -> 4
- net /HRTIM1_CHB2: track 0.00 -> 14.0 mm
- net /INP4: track 0.00 -> 13.1 mm
- net /INN4: track 0.00 -> 12.9 mm
- net /HRTIM1_CHC1: track 0.00 -> 12.7 mm
- net /VDDI4: track 0.00 -> 12.6 mm, vias 0 -> 4
- net /HRTIM1_CHB1: track 0.80 -> 13.3 mm
- net /HRTIM1_CHC2: track 0.00 -> 12.1 mm
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- added copper zone on F.Cu, net /G1
- added copper zone on F.Cu, net /G2
- added copper zone on F.Cu, net /G3
- added copper zone on F.Cu, net /G4
- added copper zone on B.Cu, net /S1
- added copper zone on B.Cu, net /S2
- added copper zone on B.Cu, net /S3
- added copper zone on B.Cu, net /VDDI1
- added copper zone on B.Cu, net /VDDI2
- added copper zone on B.Cu, net /VDDI3
- added copper zone on B.Cu, net /VDDI4
- added copper zone on B.Cu, net GND
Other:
- board size 69.3 x 36.8 mm -> 69.3 x 40 mm

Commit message: layout avanti
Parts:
- moved CISOS3 1.06 mm to (56.4, 104.8), turned to -90 degrees
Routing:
- net /S3: track 53.6 -> 68.3 mm, vias 4 -> 6
- net /VDDI4: track 12.6 -> 24.5 mm, vias 4 -> 6
- net GND: track 288.4 -> 300.1 mm, vias 206 -> 216
- net /S2: track 56.0 -> 64.9 mm
- net /VDDI3: track 15.6 -> 23.7 mm, vias 4 -> 8
- net /S1: track 54.2 -> 58.3 mm
- net Net-(CFT3-OUT): track 0.00 -> 2.22 mm
- net Net-(CFT4-OUT): track 0.00 -> 2.20 mm
- added copper zone on F.Cu, net /S3
- added copper zone on F.Cu, net /VDDI3
- added copper zone on In2.Cu, net /VDDI3
- added copper zone on In2.Cu, net /VDDI4
